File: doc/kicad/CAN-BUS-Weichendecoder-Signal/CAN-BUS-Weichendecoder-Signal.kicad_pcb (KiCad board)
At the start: 2 copper layers, 58.4 x 127 mm, 41 parts, among them J1 Conn_01x04_Male, J11 250-1406, J12 Wago 250-1406, J13 Wago 250-1406, J14 Wago 250-1406, J15 Wago 250-1406, J16 Wago 250-1406, J21 Conn_01x06, J22 Conn_01x06, J23 Conn_01x06, J24 Conn_01x06, J25 Conn_01x06, J26 Conn_01x06, J31 RJ12, J32 RJ12, J33 RJ12, J34 RJ12, J35 RJ12, J36 RJ12, J5 Conn_01x03, U1 PCF8574, U2 PCF8574, U3 PCF8574, U4 PCF8574, U5 ULN2803A, U6 ULN2803A, U7 ULN2803A, U8 ULN2803A

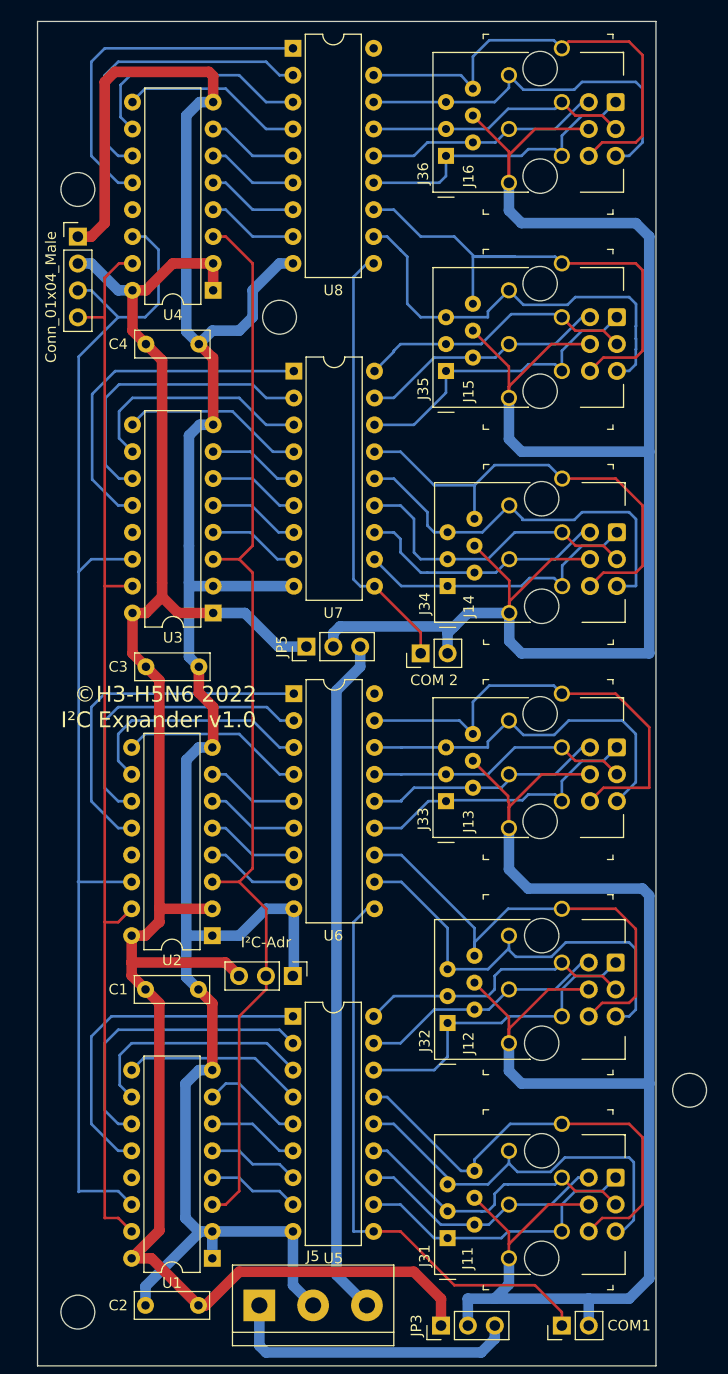
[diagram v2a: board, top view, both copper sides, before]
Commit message: Befsetigungsleucher plaziert
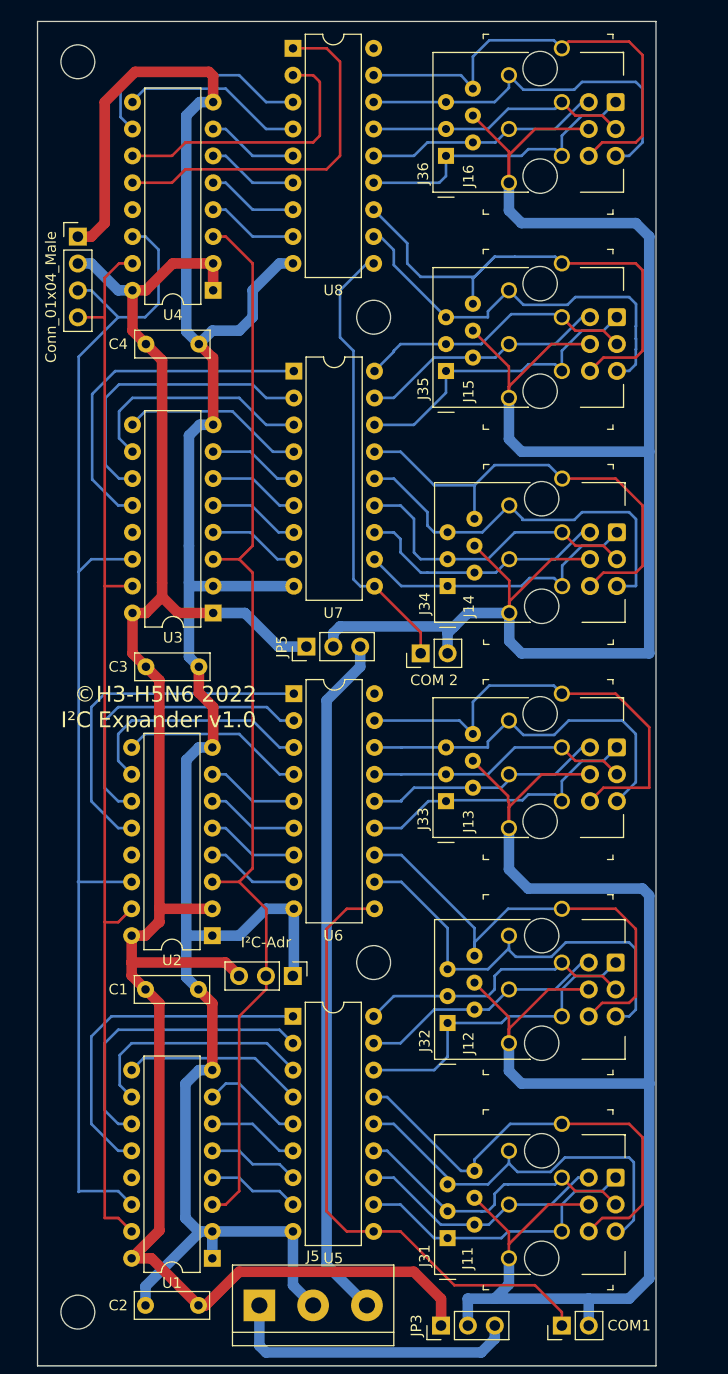
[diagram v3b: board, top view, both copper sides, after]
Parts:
- moved H4 32.2 mm to (100.3, 141.0)
- moved H3 12.1 mm to (72.4, 55.9)
- moved H1 8.89 mm to (100.3, 80.0)
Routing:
- net Net-(JP2-Pad1): track 55.8 -> 59.4 mm
- net Net-(U4-Pad11): track 28.3 -> 26.4 mm
- net Net-(J15-Pad5): track 40.8 -> 39.1 mm
- net GND: track 215.9 -> 214.8 mm
- net Net-(U4-Pad12): track 33.4 -> 34.5 mm
- net Net-(JP4-Pad1): track 41.4 -> 42.5 mm
- net Net-(J5-Pad3): track 64.4 -> 65.1 mm

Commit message: Beschriftung hinzugefügt
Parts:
- moved JP5 4.83 mm to (89.2, 111.0)
- moved JP4 4.51 mm to (100.3, 111.0)
- moved J1 0.64 mm to (73.0, 72.4)
- moved J11 0.63 mm to (113.1, 169.5)
- moved J12 0.63 mm to (113.1, 149.2)
- moved J21 0.12 mm to (123.3, 161.3)
- moved J22 0.12 mm to (123.3, 141.0)
- moved J26 0.12 mm to (123.3, 59.7)
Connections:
- net Net-(J1-Pad3) renamed SCL
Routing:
- net Net-(J14-Pad1): track 166.9 -> 140.1 mm
- net Net-(J11-Pad1): track 150.4 -> 139.0 mm
- net +5V: track 184.3 -> 179.2 mm
- net Net-(JP4-Pad1): track 42.5 -> 39.9 mm
- net Net-(J15-Pad6): track 49.1 -> 46.7 mm
- net Net-(J5-Pad3): track 65.1 -> 67.3 mm
- net Net-(J13-Pad6): track 43.6 -> 41.4 mm
- net Net-(J16-Pad6): track 44.2 -> 42.2 mm
- net Net-(J14-Pad4): track 29.0 -> 27.1 mm
- net Net-(J14-Pad6): track 43.6 -> 42.2 mm
- net Net-(J16-Pad5): track 36.4 -> 35.2 mm
- net Net-(J14-Pad5): track 37.9 -> 36.7 mm
- net Net-(J11-Pad4): track 28.3 -> 27.2 mm
- net Net-(JP1-Pad2): track 104.2 -> 105.1 mm
- net Net-(J12-Pad5): track 41.5 -> 40.8 mm
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- added copper zone on B.Cu, net GND
- added copper zone on F.Cu, net GND
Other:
- board text added: "+"
- board text added: "+5V"
- board text added: "COM"
- board text added: "Ext"
- board text added: "GND"
- board text added: "I²C"
- board text added: "SCL"
- board text added: "SDA"

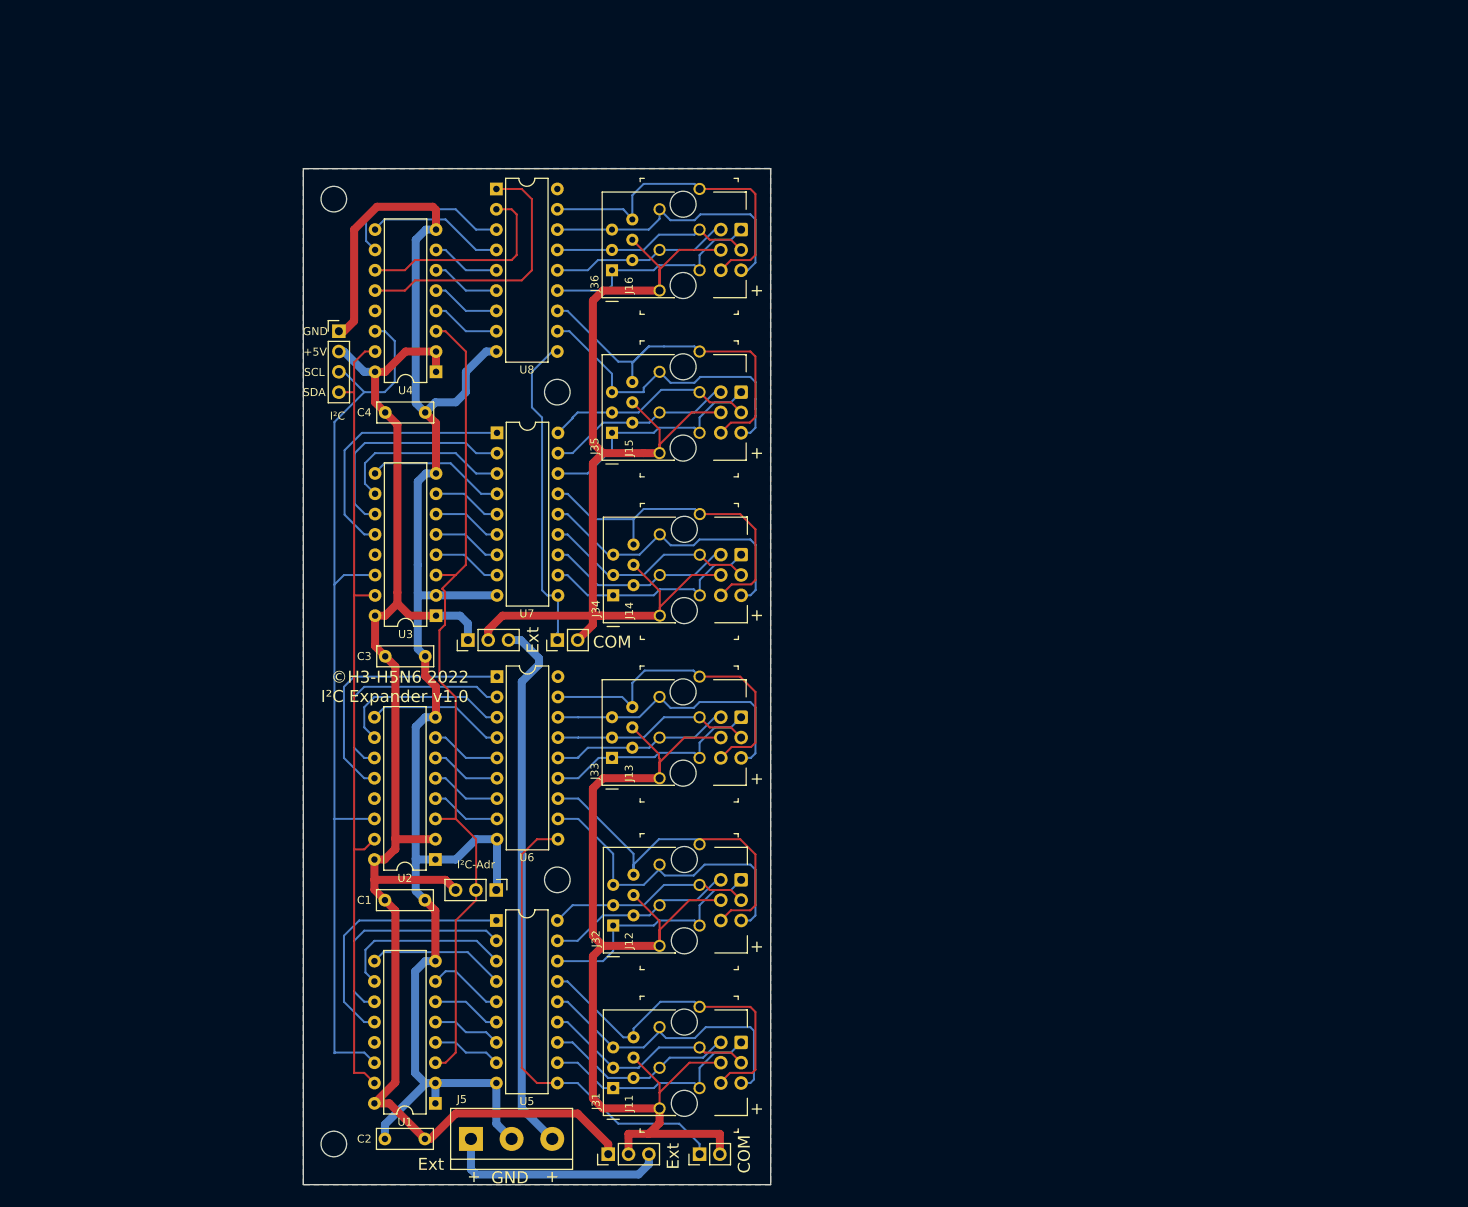
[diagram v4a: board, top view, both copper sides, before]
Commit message: Beschriftung bearbeit und Bemaßung erweitert
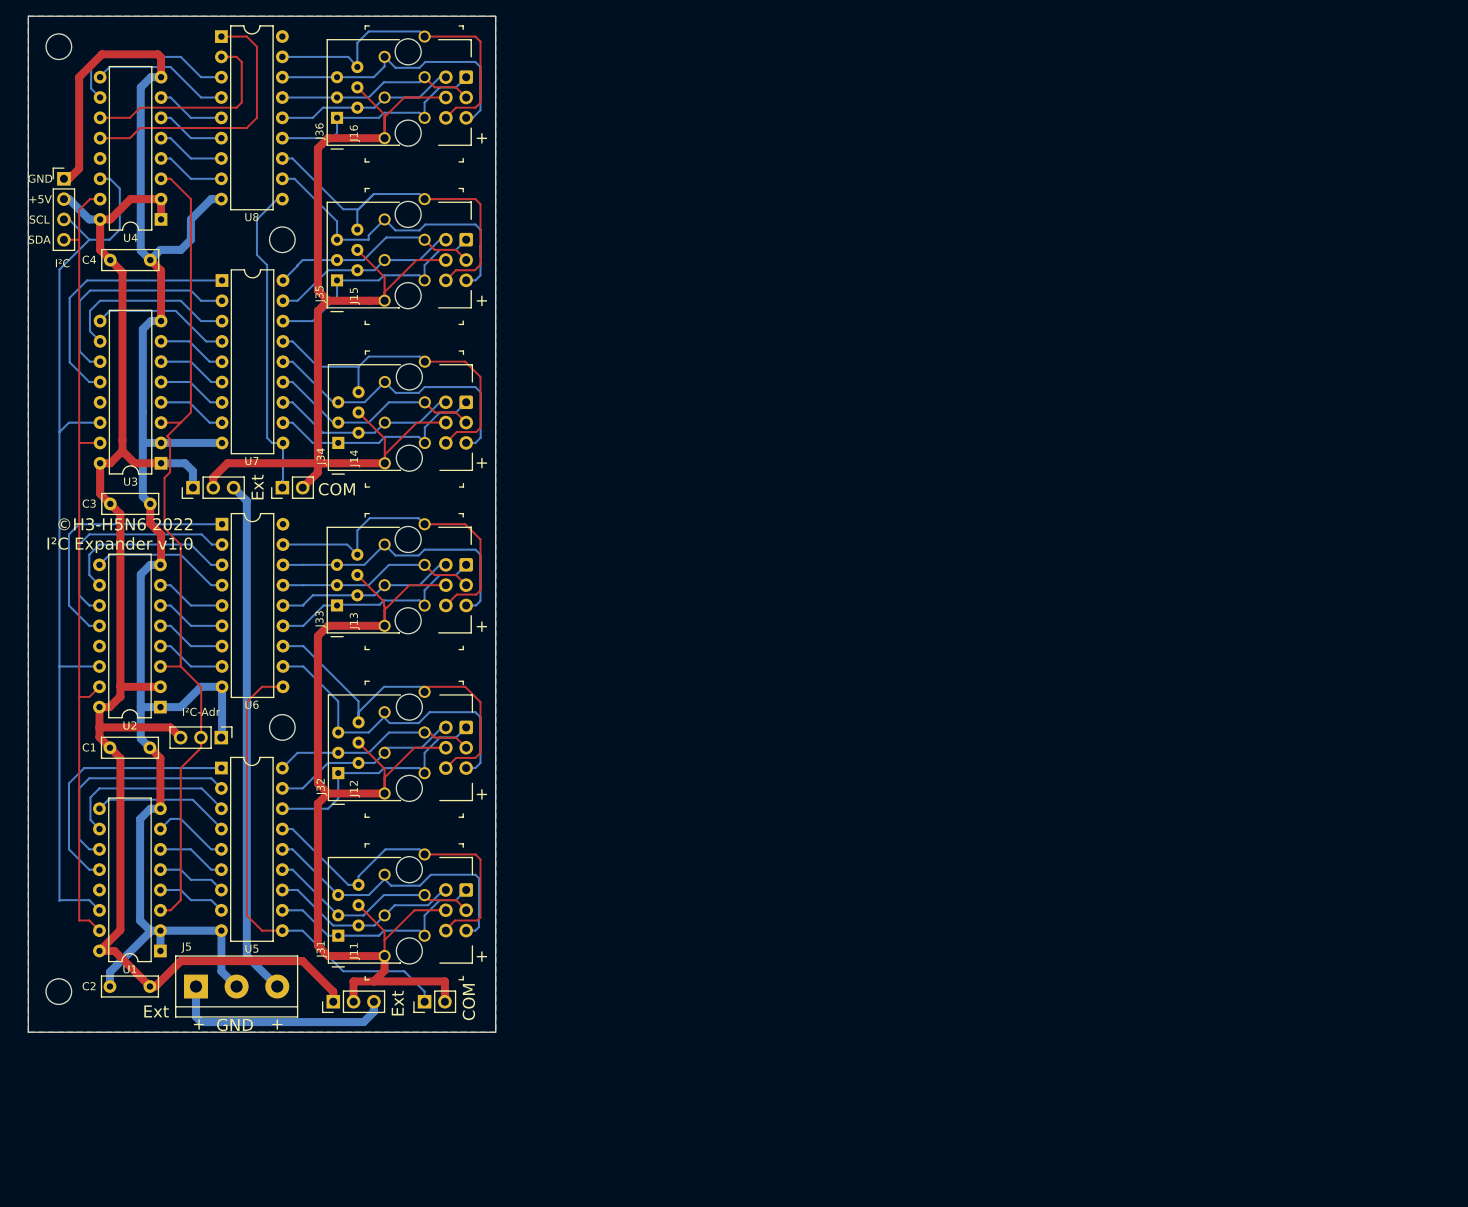
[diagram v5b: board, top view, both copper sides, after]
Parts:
- moved H1 39.3 mm to (66.0, 61.0)
- moved J13 39.3 mm to (78.7, 109.2)
- moved J16 39.3 mm to (78.7, 48.3)
- moved J31 39.3 mm to (72.9, 147.9)
- moved J32 39.3 mm to (72.9, 127.6)
- moved JP4 39.3 mm to (66.0, 91.9)
- moved U2 39.3 mm to (50.7, 119.4)
- moved C1 39.3 mm to (44.4, 124.5)
- moved H2 39.3 mm to (38.0, 154.9)
- moved H3 39.3 mm to (38.0, 36.8)
- moved H4 39.3 mm to (66.0, 121.9)
- moved J1 39.3 mm to (38.7, 53.3)
- moved J14 39.3 mm to (78.8, 88.9)
- moved J15 39.3 mm to (78.7, 68.6)
- moved J22 39.3 mm to (88.9, 121.9)
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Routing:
- net Net-(J5-Pad3): track 67.3 -> 64.6 mm
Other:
- board text added: "+1"
- board text added: "+2"
- board text added: "COM 1"
- board text added: "COM 2"
- board text added: "Ext 1"
- board text added: "Ext 2"
